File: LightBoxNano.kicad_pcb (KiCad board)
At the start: 2 copper layers, 109.8 x 109.9 mm, 70 parts, among them J5V1 Conn_02 DNP, SW1 Knitter-Switch DRR4010

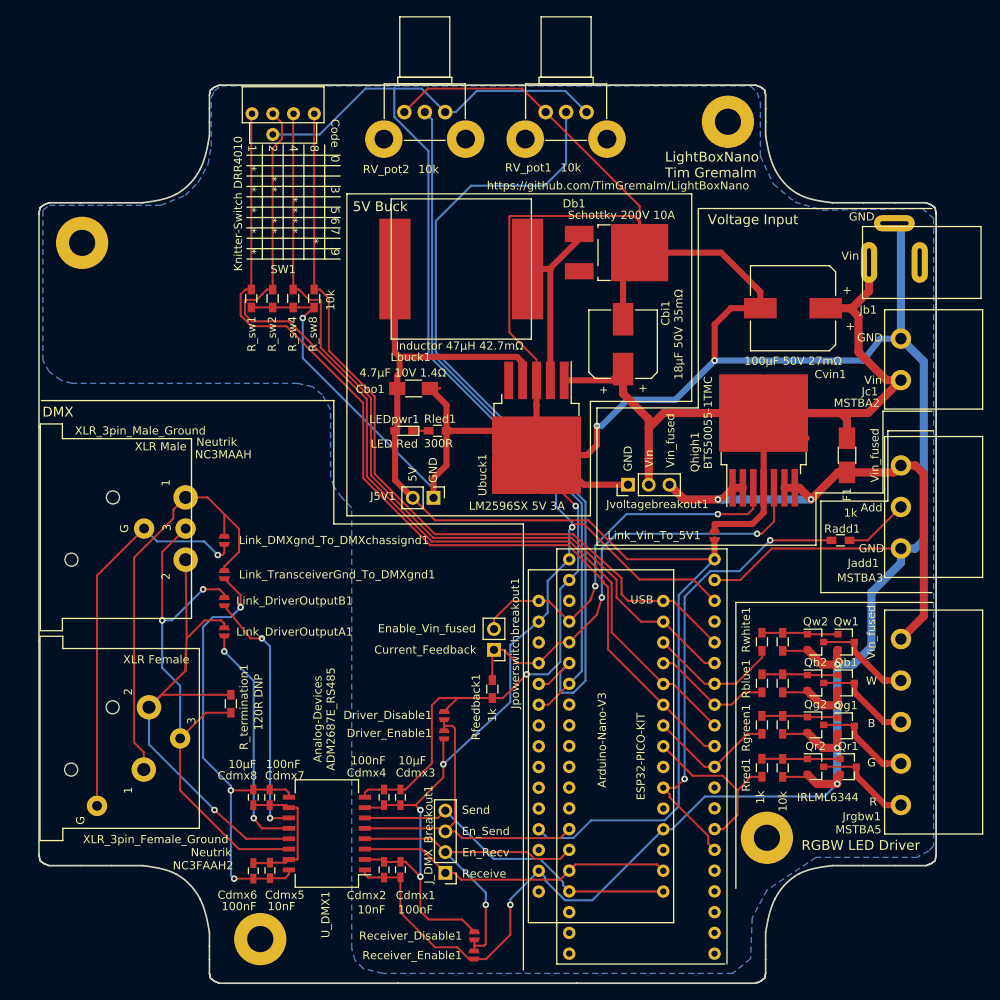
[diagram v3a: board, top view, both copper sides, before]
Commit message: Add solder prototype Area to PCB
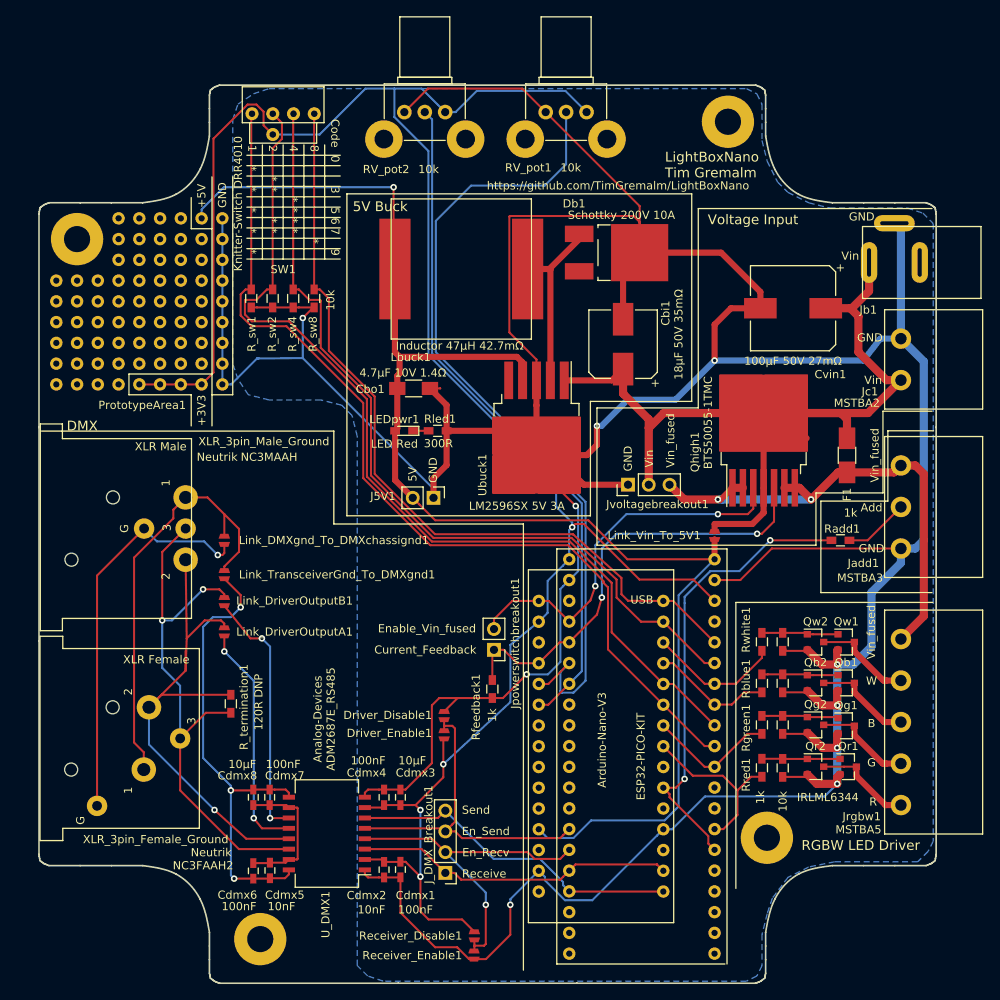
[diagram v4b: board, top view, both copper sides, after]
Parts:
- added PrototypeArea1: Conn_03, LightBoxNanoFootprints:PrototypeArea, F.Cu at (111.8, 50.8)
- moved H1 0.77 mm to (94.0, 53.3)
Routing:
- net +3V3: track 208.6 -> 258.4 mm
- net +5V: track 141.3 -> 177.1 mm, vias 0 -> 1
- net GND: track 542.3 -> 573.9 mm

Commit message: Add ESD protection diode
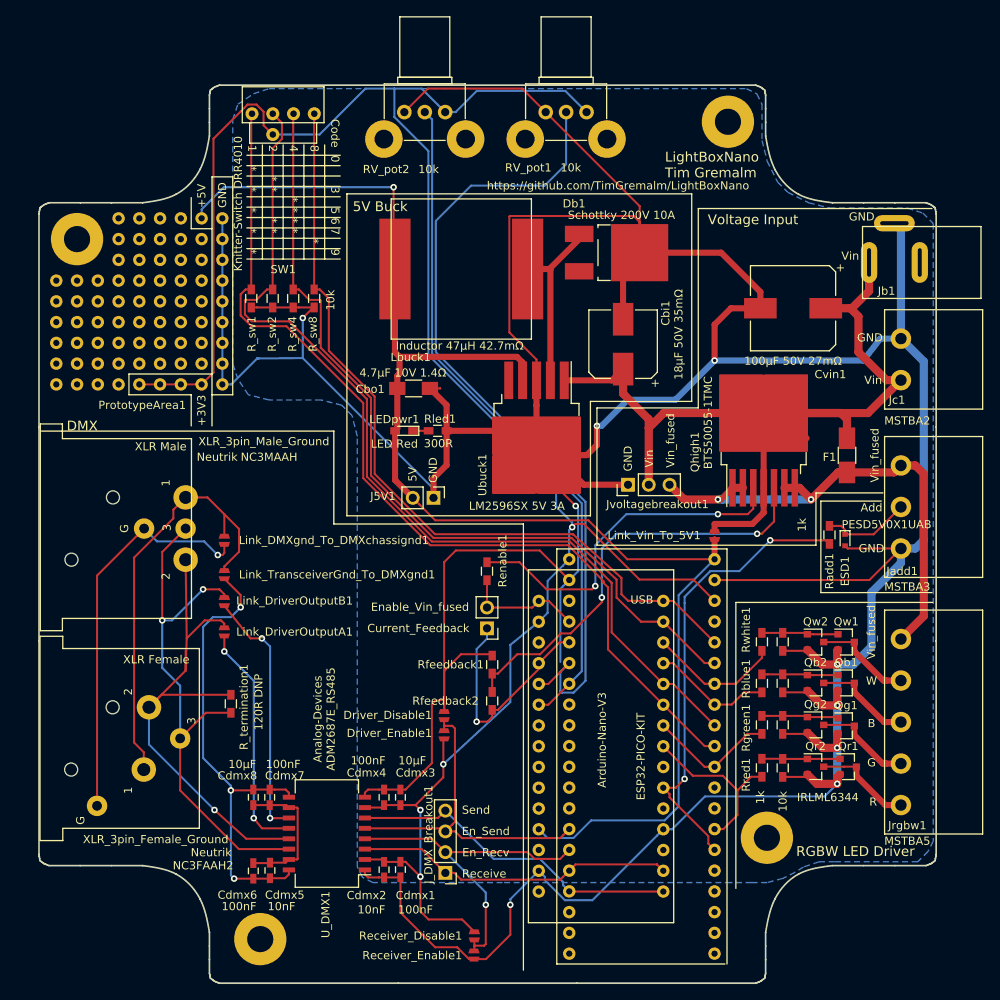
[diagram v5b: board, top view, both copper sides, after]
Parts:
- added ESD1: PESD5V0X1UAB, Diodes_SMD:D_SOD-523, F.Cu at (188.0, 90.2)
- added Renable1: 1k, Resistors_SMD:R_0603_HandSoldering, F.Cu at (144.1, 94.0)
- added Rfeedback2: 1k, Resistors_SMD:R_0603_HandSoldering, F.Cu at (144.8, 109.9)
- moved Rfeedback1 2.99 mm to (144.8, 105.4), turned to 90 degrees
- moved Jpowerswitchbreakout1 2.77 mm to (144.1, 101.0)
- moved Radd1 1.50 mm to (186.1, 89.5), turned to 270 degrees
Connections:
- Qhigh1 pad 3: /Enable_Vin_fused -> Net-(Qhigh1-Pad3)
- Qhigh1 pad 5: /Current_Feedback -> Net-(Qhigh1-Pad5)
- Rfeedback1 pad 1: /Current_Feedback -> Net-(Qhigh1-Pad5)
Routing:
- net Net-(Qhigh1-Pad5): track 0.00 -> 52.4 mm, vias 0 -> 2
- net Net-(Qhigh1-Pad3): track 0.00 -> 43.5 mm, vias 0 -> 2
- net GND: track 573.9 -> 611.3 mm, vias 10 -> 9
- net /Enable_Vin_fused: track 46.6 -> 14.8 mm, vias 2 -> 0
- net /Current_Feedback: track 54.3 -> 28.2 mm, vias 2 -> 1
- net Net-(ESD1-Pad1): track 7.99 -> 11.1 mm

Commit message: Add Led Alert logotype, layout
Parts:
- added G***: LOGO, LightBoxNanoGraphics:LedAlertLogotype, B.Cu at (160.5, 56.9)
- added REF***: OSHW-Logo_7.5x8mm_SilkScreen, Symbols:OSHW-Logo_7.5x8mm_SilkScreen, B.Cu at (119.4, 55.4)
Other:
- board text added: "C"
- board text added: "D"
- board text added: "F"
- board text added: "GPL 3.0"
- board text added: "LightBoxNano Tim Gremalm tim@gremalm.se 2020-04-13 https://github.com/TimGremalm/LightBoxNano"
- board text added: "M"
- board text added: "P"
- board text added: "S"
- board text removed: "LightBoxNano Tim Gremalm tim@gremalm.se 2020-04-10 https://github.com/TimGremalm/LightBoxNano"
